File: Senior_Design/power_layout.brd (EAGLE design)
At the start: 100 x 80 mm, 29 parts, among them IC1 MIC29302WU, J1 78646-3001, J2 292303-1, J3 640456-4, SW1 CT10-XXXX-A2, U1 SIM7000E

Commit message: Arthur's 1st Push
Annotated on Readme as 4/4/2020 11AM push
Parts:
- removed J1: 78646-3001, 78646-3001:MOLEX_78646-3001
- removed J3: 640456-4, 640456-4:TE_640456-4
- added BRD1: POCKETBEAGLE_BRD_2, e14_BeagleBoard_PocketBeagle_v1_alpha1:POCKETBEAGLE_BRD
- added J1[SIMCARD]: 78646-3001, 78646-3001:MOLEX_78646-3001
- added J3[GROVE]: 640456-4, 640456-4:TE_640456-4
- moved J2 115.2 mm to (19.1, 33.0), turned to 270 degrees
- moved U1 73.5 mm to (45.7, 29.2)
- moved IC1 33.7 mm to (11.4, 27.9), flipped to the bottom
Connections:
- net +5V: now also J3[GROVE].1; no longer J3.1
- net 0: now also J1[SIMCARD].C5, J1[SIMCARD].G1, J1[SIMCARD].G2, J1[SIMCARD].G3, J1[SIMCARD].G4, J1[SIMCARD].G5, J1[SIMCARD].G6, J3[GROVE].4; no longer J1.C5, J1.G1, J1.G2, J1.G3, J1.G4, J1.G5, J1.G6, J3.4
- net N$1: now also J1[SIMCARD].C2; no longer J1.C2
- net N$10: now also J3[GROVE].3; no longer J3.3
- net N$2: now also J1[SIMCARD].C3; no longer J1.C3
- net N$4: now also J1[SIMCARD].C1; no longer J1.C1
- net N$6: now also J1[SIMCARD].C7; no longer J1.C7
- net N$9: now also J3[GROVE].2; no longer J3.2
- net VPP: now also J1[SIMCARD].C6; no longer J1.C6
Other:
- board size 100 x 80 mm -> 55 x 35 mm

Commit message: Schematic & Layout Updates
Updates made prior to poster publishing for Demo Day Poster!
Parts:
- removed D4, D5, D6, D7: 1N4004, diode:DO41-10
- added C7: 0.1uF, capacitor-wima:C2.5-3
- added J4[GROVE]: 640456-4, 640456-4:TE_640456-4
- added R11, R12, R13, R14, R15, R16: (no value), SparkFun-Resistors:0402
- added SV1, SV2: (no value), con-lstb:MA18-2
- added SW2, SW3: (no value), adafruit:PUSHBUTTON_SMD_SJ
- added U$1: MSQA6V1W5T2G, Personal:SOT-23-5_M5
- added U2: TUSB2046BIRHBR, TUSB2046B:RHB32_3P45X3P45
- SW1: value CT10-XXXX-A2 -> (none); device switch-coto:CT10-XXXX-A2 -> adafruit:PUSHBUTTON_SMD_SJ
- moved C6 213.6 mm to (84.2, 15.4)
- moved R3 202.8 mm to (93.3, 28.9), turned to 90 degrees
- moved R9 199.6 mm to (80.9, 11.1), turned to 90 degrees
- moved R10 198.2 mm to (76.6, 11.1), turned to 270 degrees
- moved R2 194.9 mm to (86.5, 28.7), turned to 90 degrees
- moved SW1 193.3 mm to (78.5, 5.45), turned to 270 degrees
- moved R1 187.1 mm to (79.7, 28.7), turned to 90 degrees
- moved R4 183.7 mm to (73.7, 20.8), flipped to the bottom, turned to 90 degrees
- moved D1 169.3 mm to (93.2, 32.3), turned to 270 degrees
- moved D2 167.9 mm to (86.7, 32.3), turned to 270 degrees
- moved D3 166.0 mm to (79.7, 32.2), turned to 270 degrees
- moved C2 149.6 mm to (13.7, 19.2)
- moved R6 143.7 mm to (13.7, 24.2), turned to 90 degrees
- moved R5 142.8 mm to (16.4, 24.3), turned to 90 degrees
- moved R8 139.1 mm to (13.2, 10.8), turned to 90 degrees
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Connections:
- new net GND: U2.28
- new net GND_2: U2.7
- new net N$12: J4[GROVE].2, R11.1
- new net N$13: J4[GROVE].3, R12.1
- new net N$14: R13.1, SW2.P$2
- new net N$15: R15.1, SW3.P$2
- new net VCC: U2.25
- new net VCC_2: U2.3
- net +5V: now also C7.2, J4[GROVE].1, R11.2, R12.2, R13.2, R15.2
- net 0: now also C7.1, J4[GROVE].4, R14.1, R16.1, U$1.P$2; no longer D4.A, D5.A, D6.A, D7.A
- net N$1: now also C6.1, J1[SIMCARD].C1, U$1.P$5, U1.30; no longer J1[SIMCARD].C2, U1.32
- net N$11: now also SW1.P$2; no longer SW1.2
- net N$2: now also U$1.P$3; no longer D5.C, D6.C
- net N$4: now also J1[SIMCARD].C2, U$1.P$1, U1.32; no longer C6.1, D7.C, J1[SIMCARD].C1, U1.30
- net N$6: now also U$1.P$4; no longer D4.C
- net NRESET: now also R14.2, R16.2, SW1.P$1, SW2.P$1, SW3.P$1; no longer SW1.1
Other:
- board size 55 x 35 mm -> 105.8 x 35 mm

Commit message: PCB Review 2 meeting Push
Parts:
- removed IC1: MIC29302WU, MIC29302WU:TO263-5
- added C10, C11, C8, C9: (no value), rcl:C0805
- added C12, C13, C14, C15: 27pF, rcl:C0603
- added CR1: 9C-6.000MAAJ-T, Personal:CRYSTAL_TXC_9C_TXC
- added D4: Yellow, SparkFun-LED:LED-0603
- added J1: AU-Y1008-2, Personal:CONN_AU-Y1008-2_ASM
- added POWER_SUPPLY: MIC29302WU, MIC29302WU:TO263-5
- added R17: 4.7k, SparkFun-Resistors:0603
- added R18: 47k, SparkFun-Resistors:0603
- added R19, R20: 27, SparkFun-Resistors:0805
- added R21, R22: (no value), SparkFun-Resistors:0805
- added R23, R24: 15k, SparkFun-Resistors:0805
- added R25: 1.5k, SparkFun-Resistors:0805
- added R26, R27: 0, SparkFun-Resistors:0603
- added R28: 330, SparkFun-Resistors:0603
- added R29, R30, R31, R32: 4700, SparkFun-Resistors:0805
- added SJ1: (no value), jumper:SJ
- added T1, T2: BCX70SMD, transistor:SOT23
- added TP1, TP10, TP11, TP12, TP13, TP14, TP15, TP16, TP17, TP18, TP19, TP3, TP4, TP5, TP6, TP7, TP8, TP9: TPTP10R, testpad:TP10R
- added TP2: TPTP16R, testpad:TP16R
- added U3: MAX3373EEKA+T, Personal:21-0078H
- added U4: TPS2044BDR, Personal:D16_TEX
- added X1: 332-04, con-garry:332-04
- C1, C2, C3, C6, C7: device capacitor-wima:C2.5-3 -> rcl:C0805
- C4, C5: device rcl:C025-024X044 -> rcl:C0805
- D1: value (none) -> RED; device SparkFun-LED:LED_3MM-NS -> SparkFun-LED:LED-1206
- D2: value (none) -> GREEN; device SparkFun-LED:LED_3MM-NS -> SparkFun-LED:LED-1206
- D3: value (none) -> BLUE; device SparkFun-LED:LED_3MM-NS -> SparkFun-LED:LED-1206
- J2: value 292303-1 -> U.FL-R-SMT-1(01); device 292303-1:TE_292303-1 -> Personal:CONN_-SMT-1(01)
- R1, R2, R3: value (none) -> 330; device SparkFun-Resistors:0402 -> SparkFun-Resistors:0805
- R10, R14, R16, R4, R5, R6: device SparkFun-Resistors:0402 -> SparkFun-Resistors:0805
- R11: value (none) -> 47k; device SparkFun-Resistors:0402 -> SparkFun-Resistors:0603
- R12: value (none) -> 4.7k; device SparkFun-Resistors:0402 -> SparkFun-Resistors:0603
- R13, R15: value (none) -> 15k; device SparkFun-Resistors:0402 -> SparkFun-Resistors:0805
- R7, R8: value (none) -> 27; device SparkFun-Resistors:0402 -> SparkFun-Resistors:0805
- R9: value (none) -> 1.5k; device SparkFun-Resistors:0402 -> SparkFun-Resistors:0603
- U2: value TUSB2046BIRHBR -> TUSB2046BVFR; device TUSB2046B:RHB32_3P45X3P45 -> Personal:VF32_TEX
- moved J2 93.3 mm to (101.9, 29.2), turned to 312.7 degrees
- moved C5 81.5 mm to (83.8, 13.9), turned to 270 degrees
- moved R15 79.4 mm to (12.9, 13.3), turned to 0 degrees
- moved C3 78.9 mm to (86.4, 13.9), turned to 270 degrees
- moved R13 71.8 mm to (12.9, 16.2), turned to 0 degrees
- moved R4 34.3 mm to (39.5, 17.9), turned to 270 degrees
- moved R8 30.4 mm to (42.7, 18.2), turned to 0 degrees
- moved C4 29.4 mm to (37.0, 23.1), flipped to the bottom, turned to 180 degrees
- moved R7 27.6 mm to (42.7, 16.3), turned to 0 degrees
- moved R6 24.1 mm to (37.0, 17.9), flipped to the bottom, turned to 270 degrees
- moved R5 23.8 mm to (38.0, 14.1), flipped to the bottom, turned to 0 degrees
- moved R11 23.6 mm to (65.0, 10.00), flipped to the top, turned to 270 degrees
- moved C7 20.5 mm to (24.5, 8.93), flipped to the top, turned to 270 degrees
- moved R9 20.2 mm to (61.8, 17.7)
- moved R12 19.0 mm to (63.3, 10.0), flipped to the top, turned to 270 degrees
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- renumbered J3[GROVE] to GROVE1
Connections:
- removed net 0: C1.2, C2.1, C3.2, C4.2, C5.2, C6.2, C7.1, D1.A, D2.A, D3.A, GROVE1.4, IC1.3, J1[SIMCARD].C5, J1[SIMCARD].G1, J1[SIMCARD].G2, J1[SIMCARD].G3, J1[SIMCARD].G4, J1[SIMCARD].G5, J1[SIMCARD].G6, J2.4, J4[GROVE].4, R10.1, R14.1, R16.1, R4.1, R6.1, U$1.P$2, U1.17, U1.18, U1.2, U1.29, U1.39, U1.45, U1.46, U1.54, U1.58, U1.59, U1.61, U1.62, U1.63, U1.64, U1.65
- removed net GND_2: U2.7
- removed net GPIO_1: R3.2
- removed net GPIO_2: R2.2
- removed net GPIO_3: R1.2
- removed net UART_RXD: U1.10
- removed net UART_TXD: U1.9
- removed net VBAT: C3.1, C5.1, IC1.4, R5.2, R6.2, U1.55, U1.56, U1.57
- removed net VCC: U2.25
- removed net VCC_2: U2.3
- removed net WIFI_D+: J2.3
- removed net WIFI_D-: J2.2
- new net 1.8V: C9.1, U1.15, U3.3, U3.6
- new net 3.3V: C10.1, GROVE1.3, J4[GROVE].3, R17.2, R25.2, R29.2, R30.2, R31.2, R32.2, SJ1.1, SV1.14, U2.25, U2.26, U2.3, X1.1
- new net DM0: R8.1, SV1.9
- new net DP0: R7.1, SV1.11
- new net I2C1_SCL: C2.2, GROVE1.1, R29.1, SV2.9, TP11.TP
- new net I2C1_SDA: GROVE1.2, R30.1, SV2.11, TP12.TP
- new net I2C2_SCL: C7.2, J4[GROVE].1, R31.1, SV1.28, TP13.TP
- new net I2C2_SDA: J4[GROVE].2, R32.1, SV1.26, TP14.TP
- new net LED1: R3.2, SV2.6
- new net LED2: R2.2, SV2.8
- new net LED3: R1.2, SV2.10
- new net MODEM_POWER: C3.1, C5.1, POWER_SUPPLY.4, R5.2, R6.2, SJ1.2, TP5.TP, U1.55, U1.56, U1.57
- new net N$16: U3.5, X1.3
- new net N$17: R11.1, R12.2, T2.1
- new net N$18: R17.1, R18.2, T1.1
- new net N$19: R19.2, U2.15
- new net N$20: R20.2, U2.16
- new net N$22: R21.1, U2.20
- new net N$23: R22.1, U2.19
- new net N$24: TP17.TP, U1.38
- new net N$25: U2.24
- new net N$26: U2.23
- new net N$27: TP16.TP, U1.10, U3.1
- new net N$28: TP15.TP, U1.9, U3.4
- new net N$29: R28.2, U1.52
- new net N$30: D4.A, R28.1
- new net N$31: TP18.TP, U1.37
- new net OUT1: U4.15
- new net OUT2: J1.1, TP3.TP, U4.14
- new net OUT3: J1.5, TP4.TP, U4.11
- new net OUT4: U4.10
- new net OVRCUR1: U2.10, U4.16
- new net OVRCUR2: U2.14, U4.13
- new net OVRCUR3: U2.18, U4.12
- new net OVRCUR4: U2.22, U4.9
- new net PB2: R14.2, SV2.17, SW2.P$1
- new net PB3: R16.2, SV2.19, SW3.P$1
- new net PRE_ANT: C15.1, R26.2, U1.60
- new net PWRKEY: C8.1, SV2.3, T1.3, U1.1
- new net PWRON1: U2.9, U4.3
- new net PWRON2: U2.13, U4.4
- new net PWRON3: U2.17, U4.7
- new net PWRON4: U2.21, U4.8
- new net RF_ANT: J2.2, R27.1
- new net SLEEP: R12.1, SV2.2
- new net USB1_D+: J1.3, R20.1, R24.2, TP8.TP
- new net USB1_D-: J1.2, R19.1, R23.2, TP7.TP
- new net USB2_D+: J1.7, R13.2, R21.2, TP10.TP
- new net USB2_D-: J1.6, R15.2, R22.2, TP9.TP
- new net XTAL1: C12.1, CR1.1, U2.30
- new net XTAL2: R9.2, U2.29
- net +5V: now also C11.1, POWER_SUPPLY.1, POWER_SUPPLY.2, SV1.24, SW1.P$2, SW2.P$2, SW3.P$2, TP6.TP, U4.2, U4.6; no longer C2.2, C7.2, GROVE1.1, IC1.2, J2.1, J4[GROVE].1, R11.2, R12.2, R13.2, R15.2, R7.2, R8.2, R9.2
- net GND: now also C1.2, C10.2, C11.2, C12.2, C13.2, C14.2, C15.2, C2.1, C3.2, C4.2, C5.2, C6.2, C7.1, C8.2, C9.2, D1.C, D2.C, D3.C, D4.C, GROVE1.4, J1.4, J1.8, J1[SIMCARD].C5, J1[SIMCARD].G1, J1[SIMCARD].G2, J1[SIMCARD].G3, J1[SIMCARD].G4, J1[SIMCARD].G5, J1[SIMCARD].G6, J2.1, J2.3, J4[GROVE].4, POWER_SUPPLY.3, R10.1, R11.2, R13.1, R14.1, R15.1, R16.1, R18.1, R23.1, R24.1, R4.1, R6.1, SV1.15, SV2.15, T1.2, T2.2, U$1.P$2, U1.17, U1.18, U1.2, U1.29, U1.39, U1.45, U1.46, U1.54, U1.58, U1.59, U1.61, U1.62, U1.63, U1.64, U1.65, U2.27, U2.31, U2.6, U2.7, U2.8, U3.2, U3.7, U4.1, U4.5, X1.4
- net MODEM_D+: now also U2.12
- net MODEM_D-: now also U2.11
- net N$10: now also R25.1, R7.2, U2.1; no longer GROVE1.3, R8.1
- net N$11: now also C14.1, R26.1, R27.2; no longer R9.1, SW1.P$2
- net N$12: now also R8.2, U2.2; no longer J4[GROVE].2, R11.1
- net N$13: now also U3.8, X1.2; no longer J4[GROVE].3, R12.1
- net N$14: now also C13.1, CR1.2, R9.1; no longer R13.1, SW2.P$2
- net N$15: now also TP2.TP, U1.53; no longer R15.1, SW3.P$2
- net N$3: now also POWER_SUPPLY.5; no longer IC1.5
- net N$5: now also D3.A; no longer D3.K
- net N$6: now also TP19.TP
- net N$7: now also D2.A; no longer D2.K
- net N$8: now also D1.A; no longer D1.K
- net N$9: now also TP1.TP, U1.6; no longer GROVE1.2, R7.1
- net NRESET: no longer R14.2, R16.2, SW2.P$1, SW3.P$1
- net VDD_EXT: now also T2.3, U1.3; no longer U1.15
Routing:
- net 3.3V: track 0.00 -> 147.8 mm, vias 0 -> 5
- net +5V: track 0.00 -> 125.7 mm, vias 0 -> 5
- net PWRKEY: track 0.00 -> 109.7 mm, vias 0 -> 2
- net MODEM_POWER: track 0.00 -> 90.0 mm, vias 0 -> 3
- net N$22: track 0.00 -> 67.0 mm, vias 0 -> 1
- net PB3: track 0.00 -> 66.0 mm, vias 0 -> 3
- net N$23: track 0.00 -> 65.9 mm, vias 0 -> 1
- net PB2: track 0.00 -> 65.2 mm, vias 0 -> 3
- net LED1: track 0.00 -> 63.3 mm, vias 0 -> 1
- net OUT3: track 0.00 -> 58.0 mm, vias 0 -> 1
- net I2C2_SCL: track 0.00 -> 57.0 mm
- net SLEEP: track 0.00 -> 56.8 mm, vias 0 -> 2
- net N$20: track 0.00 -> 53.0 mm, vias 0 -> 3
- net OUT2: track 0.00 -> 52.0 mm, vias 0 -> 3
- net N$19: track 0.00 -> 52.0 mm, vias 0 -> 3
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- added copper zone on layer 1, net GND
- added copper zone on layer 16, net GND

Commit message: Hopefully Final Changes Pre-Alpha Purchase
*Still need to generate GERBERS*
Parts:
- added C16: 33pF, rcl:C0603K
- added J3: U.FL-R-SMT-1(01), Personal:CONN_-SMT-1(01)
- added L1: 47nH, rcl:C1608
- added TP20, TP21, TP22, TP23, TP24, TP25, TP26, TP27, TP28: TPTP10R, testpad:TP10R
- moved TP5 22.9 mm to (104.4, 21.1), flipped to the bottom
- moved TP1 15.4 mm to (94.2, 1.21), flipped to the bottom
- moved TP3 1.06 mm to (12.5, 25.6), flipped to the bottom
- moved TP6 0.36 mm to (39.3, 11.0), flipped to the bottom
- moved TP4 0.18 mm to (9.25, 26.5), flipped to the bottom
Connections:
- removed net RF_ANT: J2.2, R27.1
- new net N$21: TP21.TP, U1.7
- new net N$32: TP22.TP, U1.8
- new net N$33: TP20.TP, U1.66
- new net N$34: TP25.TP, U2.4
- new net N$35: J2.3, R27.1
- new net N$36: C16.1, J3.3, L1.2
- net GND: now also C16.2, J2.2, J3.1, J3.2, TP26.TP, TP27.TP, TP28.TP; no longer J2.3
- net MODEM_POWER: now also L1.1
- net N$25: now also TP23.TP
- net N$26: now also TP24.TP
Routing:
- net MODEM_POWER: track 90.0 -> 105.5 mm, vias 3 -> 4
- net N$9: track 17.9 -> 4.61 mm, vias 1 -> 0
- net GND: track 28.9 -> 35.5 mm
- net N$34: track 0.00 -> 5.70 mm
- net N$32: track 0.00 -> 4.79 mm
- net N$36: track 0.00 -> 4.77 mm
- net PWRON4: track 31.4 -> 35.6 mm
- net N$26: track 0.00 -> 4.07 mm
- net N$25: track 0.00 -> 4.01 mm
- net N$21: track 0.00 -> 2.98 mm
- net N$35: track 0.00 -> 2.88 mm
- net N$33: track 0.00 -> 2.74 mm
- net RF_ANT: track 2.62 -> 0.00 mm
- net PB3: track 66.0 -> 67.1 mm
- net OUT3: track 58.0 -> 57.3 mm, vias 1 -> 0
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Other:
- board size 105.8 x 35 mm -> 108.2 x 35 mm

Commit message: Added team names to pcb and created gerber files
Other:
- board text added: "Alex Minser"
- board text added: "Arthur Brazzle"
- board text added: "Janak Patel"
- board text added: "Liza Lance"
- board text added: "NCSU ECE Senior Design 2020"
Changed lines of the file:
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@@
 <?xml version="1.0" encoding="utf-8"?>
 <!DOCTYPE eagle SYSTEM "eagle.dtd">
-<eagle version="9.6.2">
+<eagle version="9.6.0">
 <drawing>
 <settings>
-<setting alwaysvectorfont="yes"/>
+<setting alwaysvectorfont="no"/>
 <setting verticaltext="up"/>
 </settings>
@@
 <layer number="31" name="tCream" color="7" fill="4" visible="yes" active="yes"/>
 <layer number="32" name="bCream" color="7" fill="5" visible="yes" active="yes"/>
-<layer number="33" name="tFinish" color="6" fill="3" visible="no" active="yes"/>
-<layer number="34" name="bFinish" color="6" fill="6" visible="no" active="yes"/>
-<layer number="35" name="tGlue" color="7" fill="4" visible="no" active="yes"/>
-<layer number="36" name="bGlue" color="7" fill="5" visible="no" active="yes"/>
-<layer number="37" name="tTest" color="7" fill="1" visible="no" active="yes"/>
-<layer number="38" name="bTest" color="7" fill="1" visible="no" active="yes"/>
+<layer number="33" name="tFinish" color="6" fill="3" visible="yes" active="yes"/>
+<layer number="34" name="bFinish" color="6" fill="6" visible="yes" active="yes"/>
+<layer number="35" name="tGlue" color="7" fill="4" visible="yes" active="yes"/>
+<layer number="36" name="bGlue" color="7" fill="5" visible="yes" active="yes"/>
+<layer number="37" name="tTest" color="7" fill="1" visible="yes" active="yes"/>
+<layer number="38" name="bTest" color="7" fill="1" visible="yes" active="yes"/>
 <layer number="39" name="tKeepout" color="4" fill="11" visible="yes" active="yes"/>
 <layer number="40" name="bKeepout" color="1" fill="11" visible="yes" active="yes"/>
@@
 <layer number="45" name="Holes" color="7" fill="1" visible="yes" active="yes"/>
 <layer number="46" name="Milling" color="3" fill="1" visible="yes" active="yes"/>
-<layer number="47" name="Measures" color="7" fill="1" visible="no" active="yes"/>
+<layer number="47" name="Measures" color="7" fill="1" visible="yes" active="yes"/>
 <layer number="48" name="Document" color="7" fill="1" visible="yes" active="yes"/>
 <layer number="49" name="Reference" color="7" fill="1" visible="yes" active="yes"/>
@@
 <wire x1="10" y1="35" x2="0" y2="25" width="0.1" layer="20" curve="90"/>
 <wire x1="98.1622" y1="-0.0254" x2="108.1622" y2="9.9746" width="0.1" layer="20" curve="90"/>
+<text x="3.2766" y="6.7056" size="0.6096" layer="21">Janak Patel</text>
+<text x="3.3528" y="5.7658" size="0.6096" layer="21">Liza Lance</text>
+<text x="3.2004" y="4.7244" size="0.6096" layer="21">Arthur Brazzle</text>
+<text x="3.3274" y="3.683" size="0.6096" layer="21">Alex Minser</text>
+<text x="0.9144" y="7.8994" size="0.6096" layer="21">NCSU ECE Senior Design 2020</text>
 </plain>
 <attributes>

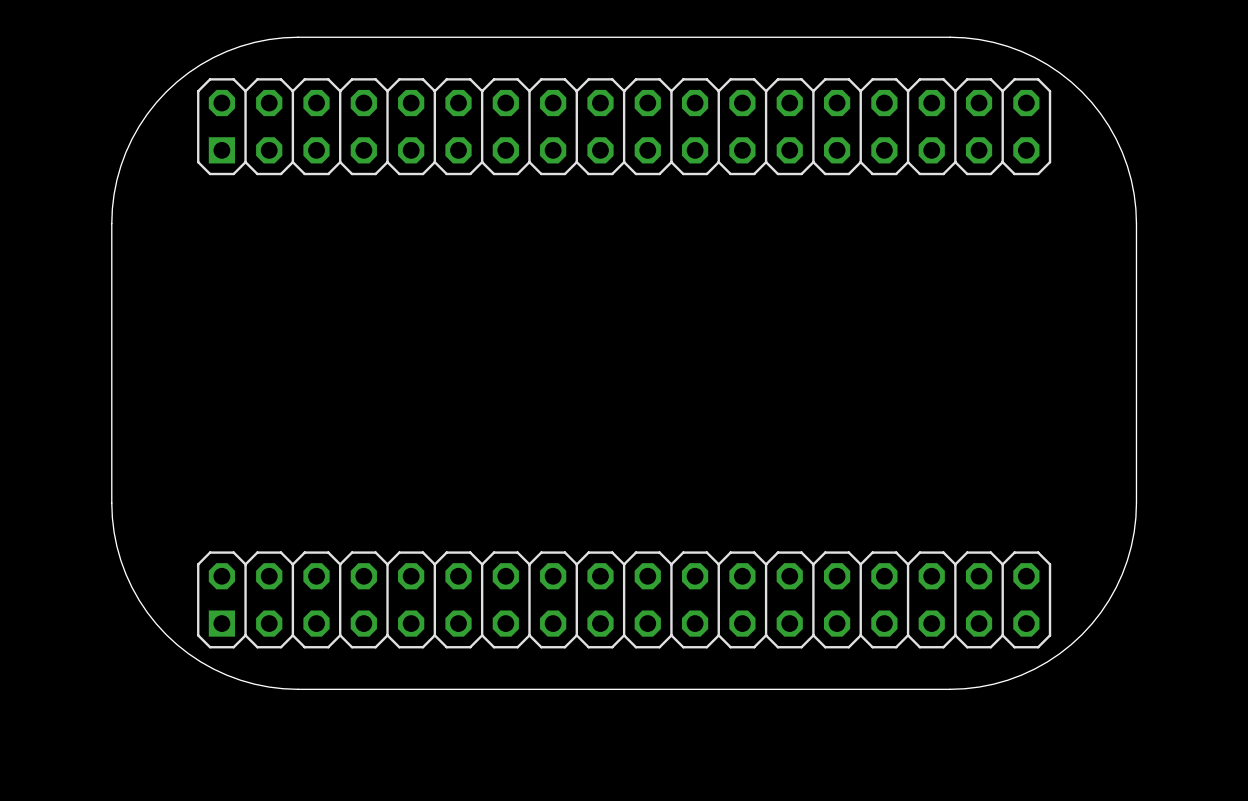
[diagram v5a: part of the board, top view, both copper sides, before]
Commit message: Fixed issues w/ gerber files
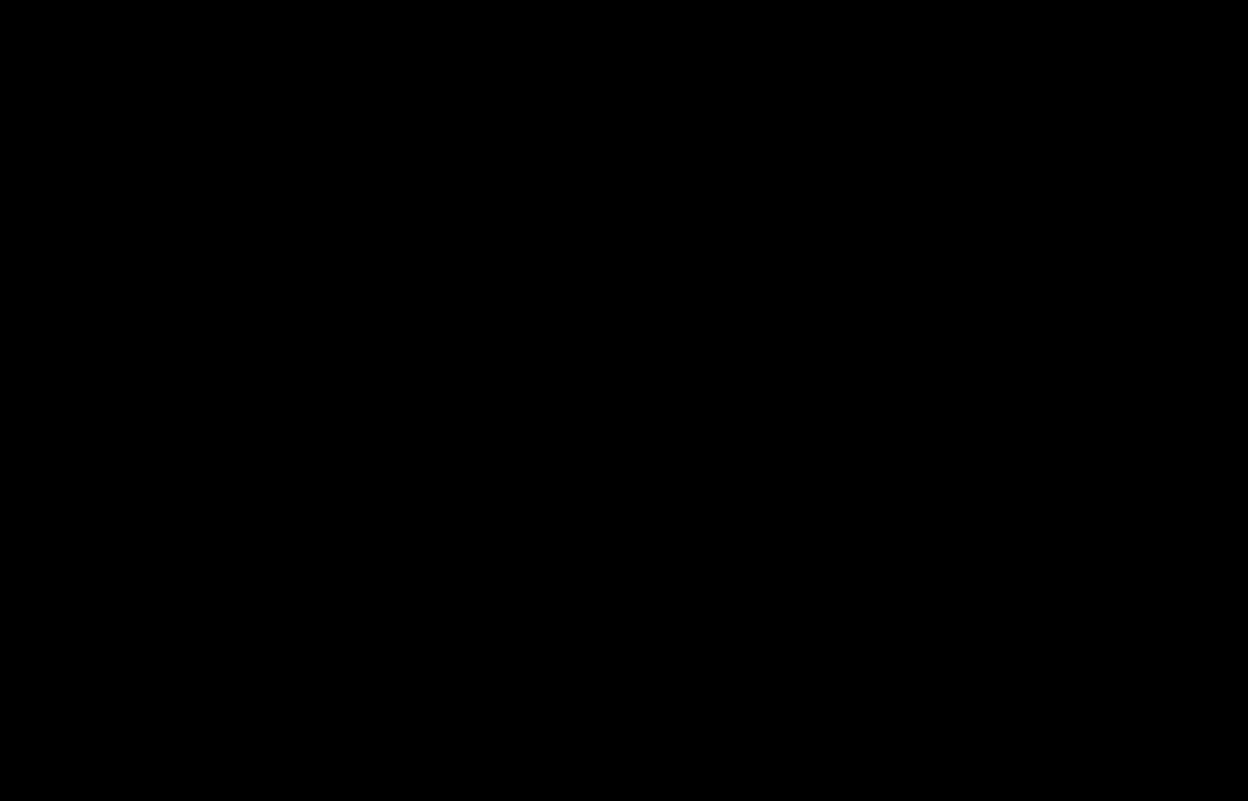
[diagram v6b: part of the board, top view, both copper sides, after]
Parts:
- removed BRD1: POCKETBEAGLE_BRD_2, e14_BeagleBoard_PocketBeagle_v1_alpha1:POCKETBEAGLE_BRD
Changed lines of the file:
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@@
 <attribute name="VALUE" x="89.027" y="22.606" size="1.27" layer="27" ratio="10"/>
 </element>
-<element name="BRD1" library="e14_BeagleBoard_PocketBeagle_v1_alpha1" package="POCKETBEAGLE_BRD" value="POCKETBEAGLE_BRD_2" x="25.12" y="46.1" smashed="yes"/>
 <element name="J4[GROVE]" library="640456-4" package="TE_640456-4" value="640456-4" x="21" y="4" smashed="yes">
 <attribute name="CENTERLINE_PITCH" value="2.54 mm[.1 in]" x="21" y="4" size="1.778" layer="27" font="vector" display="off"/>
